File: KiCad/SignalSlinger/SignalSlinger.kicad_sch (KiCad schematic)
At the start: 64 parts, among them J101 Conn_01x02, J102 Conn_01x03, J103 Conn_01x02, J104 Conn_01x02, J105 Conn_01x04, J106 Conn_01x02, J107 DB9 Female, J109 SolderJumper_2_Bridged, P101 ISP/PDI, Q101 BSS84W-7-F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

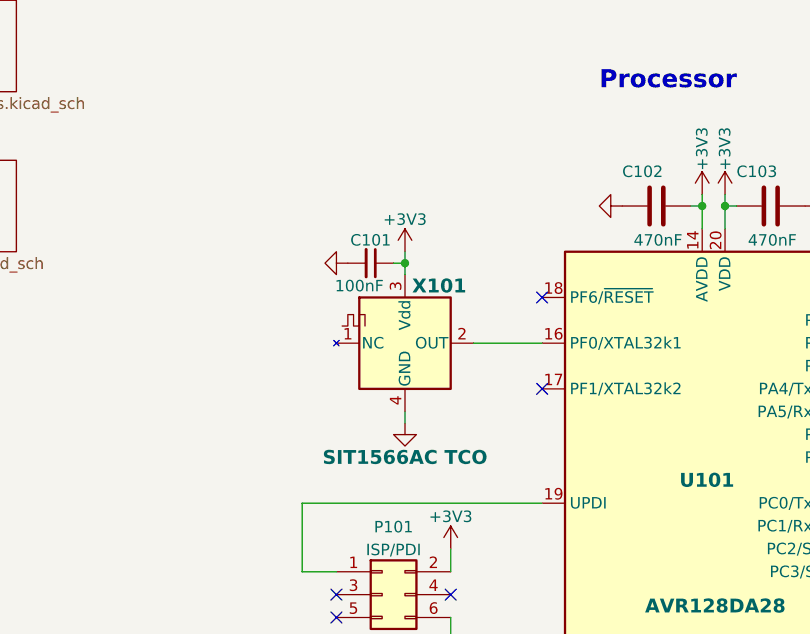
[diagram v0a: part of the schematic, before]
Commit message: Rev 2.3
Updates from initial PCB build.
Added thermal fuse F101
Support for regulated voltage
Support for charging LiPo via transmitter external power source
Updated BOM
Updated PCB and schematic
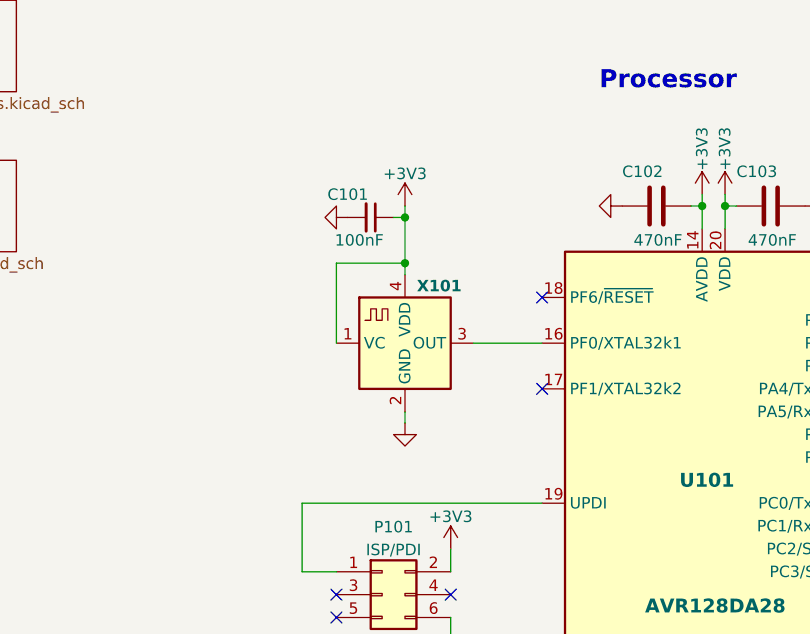
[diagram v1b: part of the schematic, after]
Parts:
- removed X101: SIT1566AC TCO, Oscillator:Oscillator_SMD_SiTime_SIT1566AC-4Pin_BGA, symbol Oscillator:SIT1566AC
- added X101: ECS-327TXO-30-TR, Oscillator:Oscillator_SMD_ECS_327TXO, symbol Oscillator:FT5HV
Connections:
- net +3V3: now also X101.1 (VC), X101.4 (VDD)
- net GND: now also X101.2 (GND)
- net at U101.16 (PF0/XTAL32k1): now also X101.3 (OUT)
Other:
- moved on the sheet: C101

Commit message: Ver 2.3
Updates to BOM information.
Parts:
- C110: value 22uF -> (none); footprint Capacitor_SMD:C_1210_3225Metric -> (none)
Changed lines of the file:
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@@
       (effects (font (size 1.27 1.27)) (justify left))
     )
-    (property "Value" "22uF" (id 1) (at 229.87 82.55 90)
+    (property "Value" "" (id 1) (at 229.87 82.55 90)
       (effects (font (size 1.27 1.27)) (justify left))
     )
-    (property "Footprint" "Capacitor_SMD:C_1210_3225Metric" (id 2) (at 227.33 80.01 0)
+    (property "Footprint" "" (id 2) (at 227.33 80.01 0)
       (effects (font (size 1.27 1.27)) hide)
     )
@@
       (reference "C212") (unit 1) (value "1uF") (footprint "Capacitor_SMD:C_0805_2012Metric")
     )
-    (path "/b7c888bf-e50e-45b8-8886-9bc5abf637fe/01d30a66-451a-43fd-95f2-0bdd2117103d"
+    (path "/b7c888bf-e50e-45b8-8886-9bc5abf637fe/5bd475aa-1807-415f-a022-e4e7bd343349"
       (reference "C213") (unit 1) (value "22uF") (footprint "Capacitor_SMD:C_0805_2012Metric")
     )
-    (path "/b7c888bf-e50e-45b8-8886-9bc5abf637fe/ebba386f-ca53-469e-b170-4c68f88638d5"
+    (path "/b7c888bf-e50e-45b8-8886-9bc5abf637fe/c2a8818a-1006-4c9c-a17a-990204a6ccc2"
       (reference "C214") (unit 1) (value "22uF") (footprint "Capacitor_SMD:C_0805_2012Metric")
     )

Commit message: Ver 2.4
Minor schematic update.
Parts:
- C110: value (none) -> 22uF; footprint (none) -> Capacitor_SMD:C_1210_3225Metric
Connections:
- net V_ext: no longer D115.2 (A)
- net at C111.1, C112.2, D113.2 (A)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: now also D115.2 (A)
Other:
- note removed: "L101: 9T (24 cm) #24 Bifilar FT-50A-43"
- moved on the sheet: C111
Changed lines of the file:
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@@
   (title_block
     (title "SignalSlinger")
-    (date "2024-04-13")
-    (rev "2.3")
+    (date "2024-04-15")
+    (rev "2.4")
   )
   (junction (at 154.94 81.28) (diameter 0) (color 0 0 0 0)
@@
   (junction (at 194.31 44.45) (diameter 0) (color 0 0 0 0)
   )
+  (junction (at 252.73 76.2) (diameter 0) (color 0 0 0 0)
+  )
   (junction (at 125.73 119.38) (diameter 0) (color 0 0 0 0)
   )
@@
   (junction (at 76.2 166.37) (diameter 0) (color 0 0 0 0)
   )
+  (junction (at 252.73 71.12) (diameter 0) (color 0 0 0 0)
+  )
   (junction (at 209.55 95.25) (diameter 0) (color 0 0 0 0)
   )
@@
     (stroke (width 0) (type default) (color 0 0 0 0))
   )
-  (wire (pts (xy 226.06 57.15) (xy 218.44 57.15))
+  (wire (pts (xy 219.71 57.15) (xy 218.44 57.15))
     (stroke (width 0) (type default) (color 0 0 0 0))
   )
@@
     (stroke (width 0) (type default) (color 0 0 0 0))
   )
+  (wire (pts (xy 252.73 76.2) (xy 252.73 83.82))
+    (stroke (width 0) (type default) (color 0 0 0 0))
+  )
   (wire (pts (xy 114.3 168.91) (xy 114.3 172.72))
     (stroke (width 0) (type default) (color 0 0 0 0))
@@
     (stroke (width 0) (type default) (color 0 0 0 0))
   )
+  (wire (pts (xy 196.85 34.29) (xy 196.85 31.75))
+    (stroke (width 0) (type default) (color 0 0 0 0))
+  )
   (wire (pts (xy 76.2 171.45) (xy 76.2 173.99))
     (stroke (width 0) (type default) (color 0 0 0 0))
@@
     (stroke (width 0) (type default) (color 0 0 0 0))
   )
+  (wire (pts (xy 250.19 76.2) (xy 252.73 76.2))
+    (stroke (width 0) (type default) (color 0 0 0 0))
+  )
   (wire (pts (xy 36.83 73.66) (xy 44.45 73.66))
     (stroke (width 0) (type default) (color 0 0 0 0))
@@
     (stroke (width 0) (type default) (color 0 0 0 0))
   )
+  (wire (pts (xy 252.73 71.12) (xy 252.73 76.2))
+    (stroke (width 0) (type default) (color 0 0 0 0))
+  )
   (wire (pts (xy 21.59 99.06) (xy 17.78 99.06))
     (stroke (width 0) (type default) (color 0 0 0 0))
@@
     (stroke (width 0) (type default) (color 0 0 0 0))
   )
+  (wire (pts (xy 232.41 71.12) (xy 252.73 71.12))
+    (stroke (width 0) (type default) (color 0 0 0 0))
+  )
   (wire (pts (xy 76.2 193.04) (xy 76.2 191.77))
     (stroke (width 0) (type default) (color 0 0 0 0))
@@
     (stroke (width 0) (type default) (color 0 0 0 0))
   )
+  (wire (pts (xy 232.41 31.75) (xy 232.41 71.12))
+    (stroke (width 0) (type default) (color 0 0 0 0))
+  )
   (wire (pts (xy 80.01 93.98) (xy 115.57 93.98))
     (stroke (width 0) (type default) (color 0 0 0 0))
@@
     (stroke (width 0) (type default) (color 0 0 0 0))
   )
-  (wire (pts (xy 250.19 62.23) (xy 252.73 62.23))
-    (stroke (width 0) (type default) (color 0 0 0 0))
-  )
   (wire (pts (xy 148.59 144.78) (xy 148.59 146.05))
     (stroke (width 0) (type default) (color 0 0 0 0))
@@
     (stroke (width 0) (type default) (color 0 0 0 0))
   )
+  (wire (pts (xy 196.85 31.75) (xy 232.41 31.75))
+    (stroke (width 0) (type default) (color 0 0 0 0))
+  )
   (wire (pts (xy 260.35 57.15) (xy 260.35 58.42))
     (stroke (width 0) (type default) (color 0 0 0 0))
@@
     (stroke (width 0) (type default) (color 0 0 0 0))
   )
-  (wire (pts (xy 252.73 62.23) (xy 252.73 83.82))
+  (wire (pts (xy 252.73 62.23) (xy 252.73 71.12))
     (stroke (width 0) (type default) (color 0 0 0 0))
   )
@@
     (effects (font (size 1.27 1.27)) (justify left bottom))
   )
-  (text "L101:\n9T (24 cm) #24 Bifilar FT-50A-43" (at 254 78.74 0)
-    (effects (font (size 0.9906 0.9906) (thickness 0.1981) bold) (justify left bottom))
-  )
   (text "I2C pull-ups can be provided by uC \nport pin pull-ups on SCL and SDA."
     (at 154.94 88.9 0)
@@
     (effects (font (size 1.27 1.27)) (justify left bottom))
   )
-  (text "V = 1.25(1 + R2/R1)" (at 234.95 73.66 0)
+  (text "V = 1.25(1 + R2/R1)" (at 234.95 69.85 0)
     (effects (font (size 1 1) (thickness 0.2) bold) (justify left bottom))
   )
@@
     )
   )
-  (global_label "FET_DRIVER_ENABLE" (shape input) (at 226.06 57.15 0) (fields_autoplaced)
-    (effects (font (size 0.9906 0.9906)) (justify left))
-    (property "Intersheet References" "${INTERSHEET_REFS}" (id 0) (at 142.24 -2.54 0)
+  (global_label "FET_DRIVER_ENABLE" (shape input) (at 219.71 57.15 270) (fields_autoplaced)
+    (effects (font (size 0.9906 0.9906)) (justify right))
+    (property "Intersheet References" "${INTERSHEET_REFS}" (id 0) (at 279.4 -26.67 0)
       (effects (font (size 1.27 1.27)) hide)
     )
@@
     (pin "9")
   )
-  (symbol (lib_id "power:GND") (at 245.11 62.23 270) (unit 1)
+  (symbol (lib_id "power:GND") (at 245.11 76.2 270) (unit 1)
     (in_bom yes) (on_board yes) (fields_autoplaced)
-    (property "Reference" "#PWR0148" (id 0) (at 238.76 62.23 0)
+    (property "Reference" "#PWR0148" (id 0) (at 238.76 76.2 0)
       (effects (font (size 1.27 1.27)) hide)
     )
-    (property "Value" "GND" (id 1) (at 240.6666 62.23 0)
+    (property "Value" "GND" (id 1) (at 240.6666 76.2 0)
       (effects (font (size 1.27 1.27)) hide)
     )
-    (property "Footprint" "" (id 2) (at 245.11 62.23 0)
+    (property "Footprint" "" (id 2) (at 245.11 76.2 0)
       (effects (font (size 1.27 1.27)) hide)
     )
-    (property "Datasheet" "" (id 3) (at 245.11 62.23 0)
+    (property "Datasheet" "" (id 3) (at 245.11 76.2 0)
       (effects (font (size 1.27 1.27)) hide)
     )
@@
       (effects (font (size 1.27 1.27)) (justify left))
     )
-    (property "Value" "" (id 1) (at 229.87 82.55 90)
+    (property "Value" "22uF" (id 1) (at 229.87 82.55 90)
       (effects (font (size 1.27 1.27)) (justify left))
     )
-    (property "Footprint" "" (id 2) (at 227.33 80.01 0)
+    (property "Footprint" "Capacitor_SMD:C_1210_3225Metric" (id 2) (at 227.33 80.01 0)
       (effects (font (size 1.27 1.27)) hide)
     )
@@
     (pin "2")
   )
-  (symbol (lib_id "Device:CP1_Small-Device") (at 247.65 62.23 270) (unit 1)
+  (symbol (lib_id "Device:CP1_Small-Device") (at 247.65 76.2 270) (unit 1)
     (in_bom yes) (on_board yes)
-    (property "Reference" "C111" (id 0) (at 247.65 59.69 90))
-    (property "Value" "47uF low ESR" (id 1) (at 245.11 66.04 90))
-    (property "Footprint" "Capacitors:C_2917" (id 2) (at 247.65 62.23 0)
+    (property "Reference" "C111" (id 0) (at 247.65 73.66 90))
+    (property "Value" "47uF low ESR" (id 1) (at 245.11 78.74 90))
+    (property "Footprint" "Capacitors:C_2917" (id 2) (at 247.65 76.2 0)
       (effects (font (size 1.27 1.27)) hide)
     )
-    (property "Datasheet" "" (id 3) (at 247.65 62.23 0)
+    (property "Datasheet" "" (id 3) (at 247.65 76.2 0)
       (effects (font (size 1.27 1.27)) hide)
     )
-    (property "Digi-Key Part No." "399-3904-1-ND" (id 4) (at 247.65 62.23 0)
+    (property "Digi-Key Part No." "399-3904-1-ND" (id 4) (at 247.65 76.2 0)
       (effects (font (size 1.27 1.27)) hide)
     )
-    (property "Link" "https://www.digikey.com/products/en?keywords=399-3904-1-ND" (id 5) (at 247.65 62.23 0)
+    (property "Link" "https://www.digikey.com/products/en?keywords=399-3904-1-ND" (id 5) (at 247.65 76.2 0)
       (effects (font (size 1.524 1.524)) hide)
     )
-    (property "Manufacturer" "KEMET" (id 6) (at 247.65 62.23 90)
+    (property "Manufacturer" "KEMET" (id 6) (at 247.65 76.2 90)
       (effects (font (size 1.27 1.27)) hide)
     )
-    (property "Manufacturer PN" "T495X476K020ATE150" (id 7) (at 247.65 62.23 90)
+    (property "Manufacturer PN" "T495X476K020ATE150" (id 7) (at 247.65 76.2 90)
       (effects (font (size 1.27 1.27)) hide)
     )
-    (property "Description" "CAP TANT 47UF 10% 20V 2917" (id 8) (at 247.65 62.23 90)
+    (property "Description" "CAP TANT 47UF 10% 20V 2917" (id 8) (at 247.65 76.2 90)
       (effects (font (size 1.27 1.27)) hide)
     )
-    (property "LCSC Part Number" "C122333" (id 9) (at 247.65 62.23 0)
+    (property "LCSC Part Number" "C122333" (id 9) (at 247.65 76.2 0)
       (effects (font (size 1.27 1.27)) hide)
     )
@@
     (pin "2")
   )
-  (symbol (lib_id "power:V_ext") (at 196.85 34.29 0) (unit 1)
-    (in_bom yes) (on_board yes)
-    (property "Reference" "#PWR0138" (id 0) (at 196.85 36.83 0)
-      (effects (font (size 1.27 1.27)) hide)
-    )
-    (property "Value" "V_ext" (id 1) (at 196.85 30.7142 0))
-    (property "Footprint" "" (id 2) (at 196.85 34.29 0)
-      (effects (font (size 1.27 1.27)) hide)
-    )
-    (property "Datasheet" "" (id 3) (at 196.85 34.29 0)
-      (effects (font (size 1.27 1.27)) hide)
-    )
-    (pin "1")
-  )
   (symbol (lib_id "power:GND") (at 62.23 132.08 0) (unit 1)
     (in_bom yes) (on_board yes)
@@
       (reference "#PWR0137") (unit 1) (value "GND") (footprint "")
     )
-    (path "/b8fdcd31-a1bd-46e4-bcaf-5134458969ca"
-      (reference "#PWR0138") (unit 1) (value "V_ext") (footprint "")
-    )
     (path "/12358390-7579-43ca-ab80-73800a1251a5"

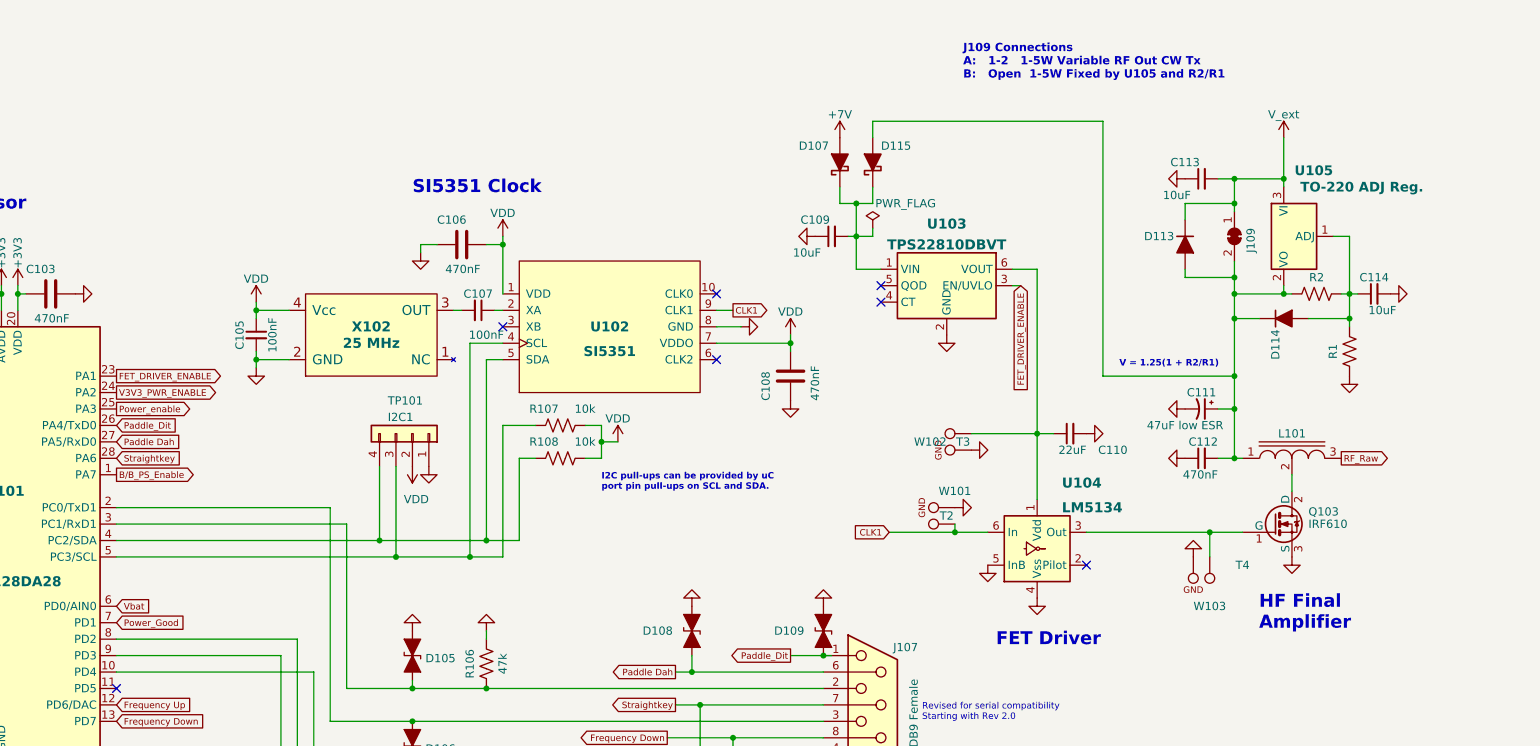
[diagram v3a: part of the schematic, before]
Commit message: Added voltage divider
Now supports monitoring external battery voltage.
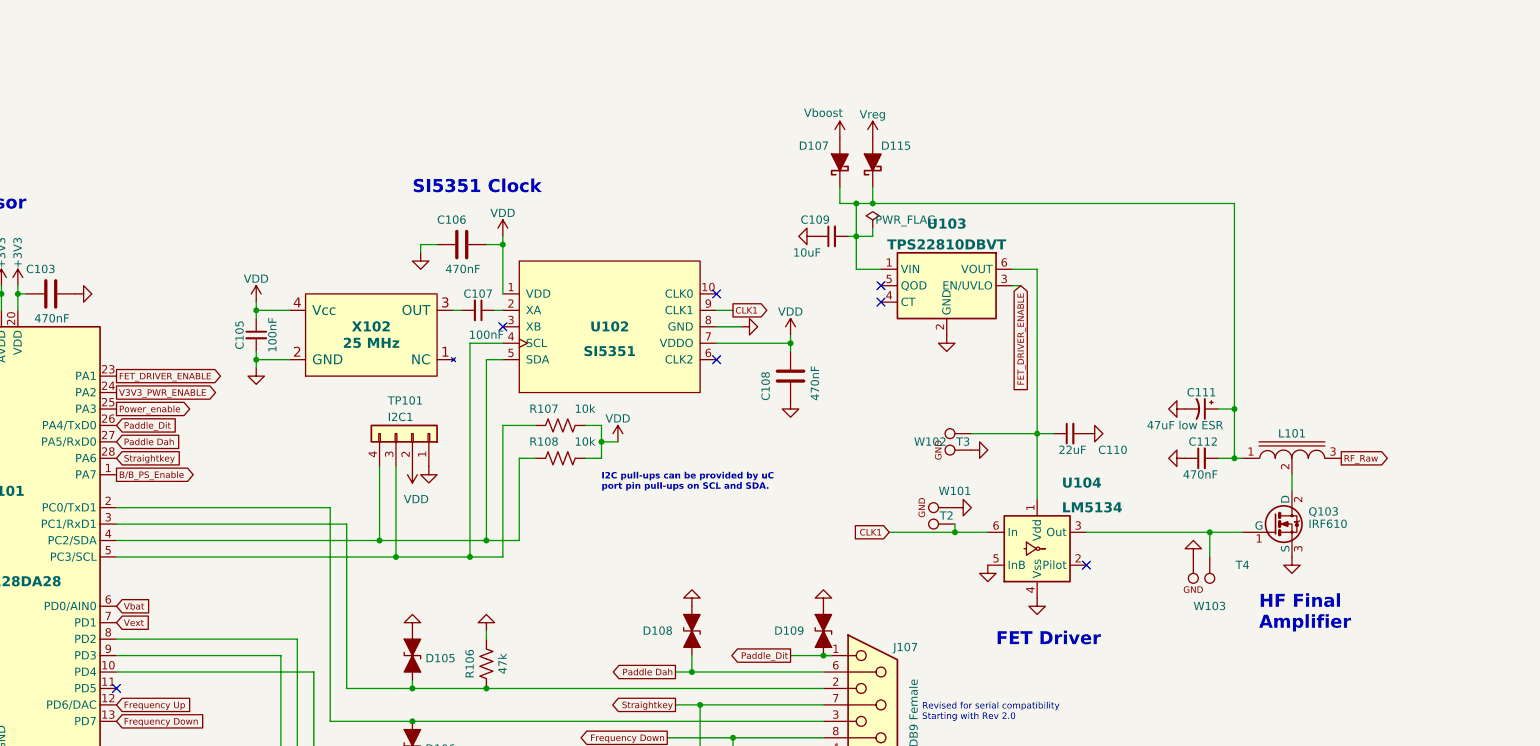
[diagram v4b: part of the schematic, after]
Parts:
- removed C113, C114: 10uF, Capacitor_SMD:C_0805_2012Metric, symbol Device:C_Small
- removed D113, D114: 1N4001, Diode_SMD:D_SOD-123F, symbol Diode:1N914WT
- removed J109: SolderJumper_2_Bridged, Jumper:SolderJumper-2_P1.3mm_Bridged_RoundedPad1.0x1.5mm, symbol Jumper:SolderJumper_2_Bridged
- removed R1, R2: TBD, Resistor_THT:R_Axial_DIN0204_L3.6mm_D1.6mm_P2.54mm_Vertical, symbol Device:R_Small_US
- removed U105: TO-220 ADJ Reg., TO_SOT_Packages:TO-220_Neutral123_Horizontal, symbol Regulator_Linear:LT1086-ADJ
- D104: footprint LED_SMD:LED_APDA1806SECK -> LED_SMD:LED_0805_2012Metric
- L101: footprint Inductors:Toroid_T-50A_TH_BF_CT -> Inductors:Toroid_T-50A_TH_BF_CT_Vertical
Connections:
- net at C109.2, D107.1 (K), D115.1 (K)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: now also C111.1, C112.2, L101.1
- net +7V renamed Vdrive
- net Vdrive: now also D115.2 (A)
- net Power_Good renamed Vext
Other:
- note removed: "J109 Connections A: 1-2 1-5W Variable RF Out CW Tx B: Open 1-5W Fixed by U105 and R2/R1"
- note removed: "V = 1.25(1 + R2/R1)"
